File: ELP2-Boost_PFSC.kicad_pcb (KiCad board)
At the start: 2 copper layers, 130 x 150 mm, 44 parts, among them J1 Screw_Terminal_01x03, J2 Screw_Terminal_01x03, Q1 12n50C3, U1 UCC38050

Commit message: Placa refeita de acordo com pedidos do professor, sujeita a alteração
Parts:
- removed RV1: R_Potentiometer_Trim, ELP-Boost_PFC:Trimpot-10k
- added Rs1: 270m, Resistor_SMD:R_2512_6332Metric_Pad1.40x3.35mm_HandSolder, B.Cu at (144.2, 100.8)
- C1, C2, C3, C6: footprint Capacitor_THT:C_Disc_D5.0mm_W2.5mm_P2.50mm -> Capacitor_THT:C_Disc_D5.0mm_W2.5mm_P5.00mm
- C4: footprint Capacitor_THT:C_Rect_L9.0mm_W2.5mm_P7.50mm_MKT -> Capacitor_THT:C_Disc_D5.0mm_W2.5mm_P5.00mm
- C5: footprint Capacitor_THT:C_Rect_L13.5mm_W5.0mm_P10.00mm_FKS3_FKP3_MKS4 -> Capacitor_THT:C_Disc_D5.0mm_W2.5mm_P5.00mm
- C7: footprint Capacitor_THT:C_Rect_L7.2mm_W3.5mm_P5.00mm_FKS2_FKP2_MKS2_MKP2 -> Capacitor_THT:C_Rect_L31.5mm_W9.0mm_P27.50mm_MKS4
- R11, R12, R13: footprint Resistor_THT:R_Axial_DIN0207_L6.3mm_D2.5mm_P15.24mm_Horizontal -> Resistor_THT:R_Axial_DIN0207_L6.3mm_D2.5mm_P10.16mm_Horizontal
- TP1: value TestPoint -> Current_Sense
- moved TP1 86.7 mm to (137.0, 126.1), turned to 90 degrees
- moved C2 76.5 mm to (141.6, 122.1)
- moved R6 71.2 mm to (109.1, 106.4), turned to -90 degrees
- moved TP2 67.5 mm to (103.1, 107.1), turned to 0 degrees
- moved R5 64.3 mm to (138.8, 108.4), turned to 90 degrees
- moved C5 61.5 mm to (146.0, 117.4), turned to 0 degrees
- moved R7 61.1 mm to (109.0, 103.2), turned to 90 degrees
- moved J2 57.5 mm to (151.4, 66.1), turned to 90 degrees
- moved R3 55.4 mm to (148.0, 143.8), turned to -90 degrees
- moved R4 51.3 mm to (109.0, 89.5), turned to 90 degrees
- moved C4 51.1 mm to (145.9, 122.3)
- moved C1 45.8 mm to (142.7, 144.1), turned to -90 degrees
- moved R2 45.6 mm to (134.5, 154.6), turned to 180 degrees
- moved R9 40.3 mm to (151.0, 136.0), turned to 90 degrees
- moved R10 35.9 mm to (122.9, 121.8), turned to 90 degrees
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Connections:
- R6 pad 2: Net-(R6-Pad2) -> Earth
- TR1 pad 1: Net-(D6-A) -> /ZCD
- TR1 pad 5: Net-(D5-+) -> Earth
- TR1 pad 7: Earth -> Net-(D6-A)
- TR1 pad 9: /ZCD -> Net-(D5-+)
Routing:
- net /PFC/VO_SNS: track 168.8 -> 57.0 mm
- net /PFC/Current_Sense: track 119.5 -> 25.6 mm, vias 2 -> 0
- net Net-(D5-+): track 181.2 -> 90.3 mm
- net Earth: track 322.7 -> 253.1 mm, vias 2 -> 0
- net /PFC/Comp: track 76.2 -> 13.2 mm
- net /Vcc: track 49.0 -> 88.2 mm, vias 2 -> 0
- net Net-(D6-A): track 39.7 -> 67.2 mm
- net Net-(R1-Pad1): track 5.60 -> 32.7 mm
- net /ZCD: track 78.6 -> 53.2 mm
- net /PWM: track 26.6 -> 3.71 mm
- net /PFC/Zero_Cross: track 25.5 -> 9.57 mm
- net Net-(D7-K): track 13.7 -> 28.8 mm
- net /Out+: track 54.1 -> 68.0 mm
- net /CS: track 0.00 -> 10.0 mm
- net /PFC/Mult_In: track 61.7 -> 51.7 mm, vias 2 -> 0
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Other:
- board text removed: "Alimentação - Vcc"
- board text removed: "Compensador"
- board text removed: "Current Sense"
- board text removed: "Driver"
- board text removed: "Fechamento da Malha - 2,5V @ 400V Saída"
- board text removed: "Realimentação"
- board text removed: "Vo_SNS"
- board text removed: "Zero Cross"

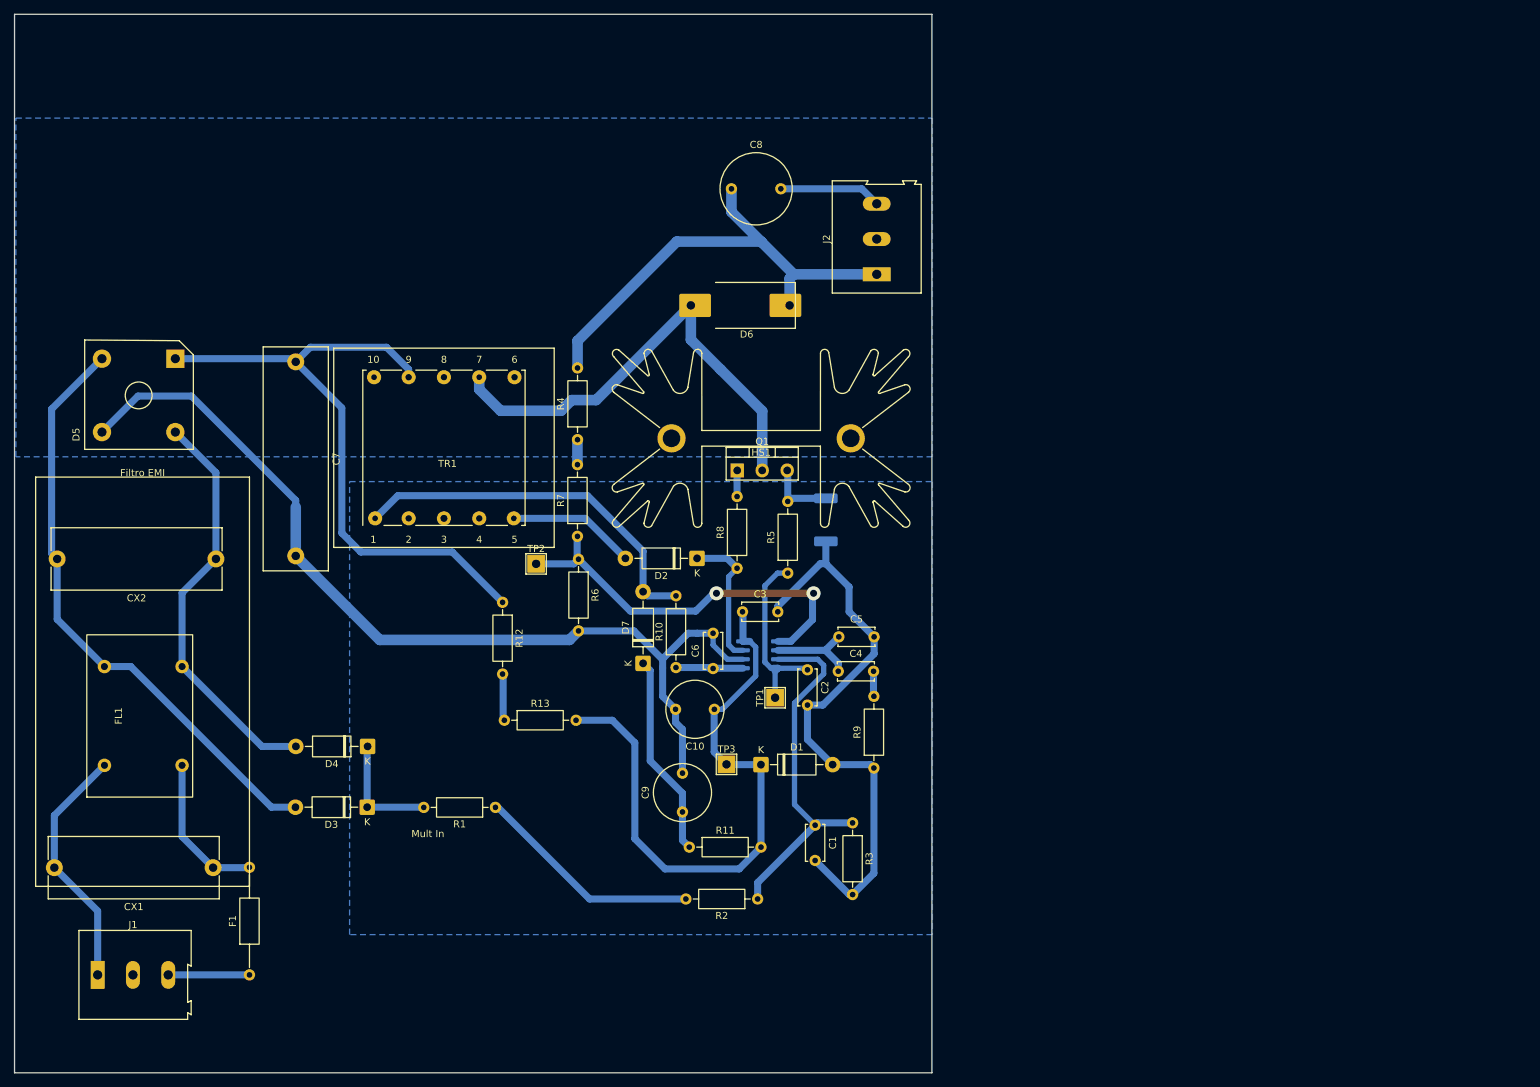
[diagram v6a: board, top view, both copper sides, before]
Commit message: Ajustes nos planos de referência e posição do shunt
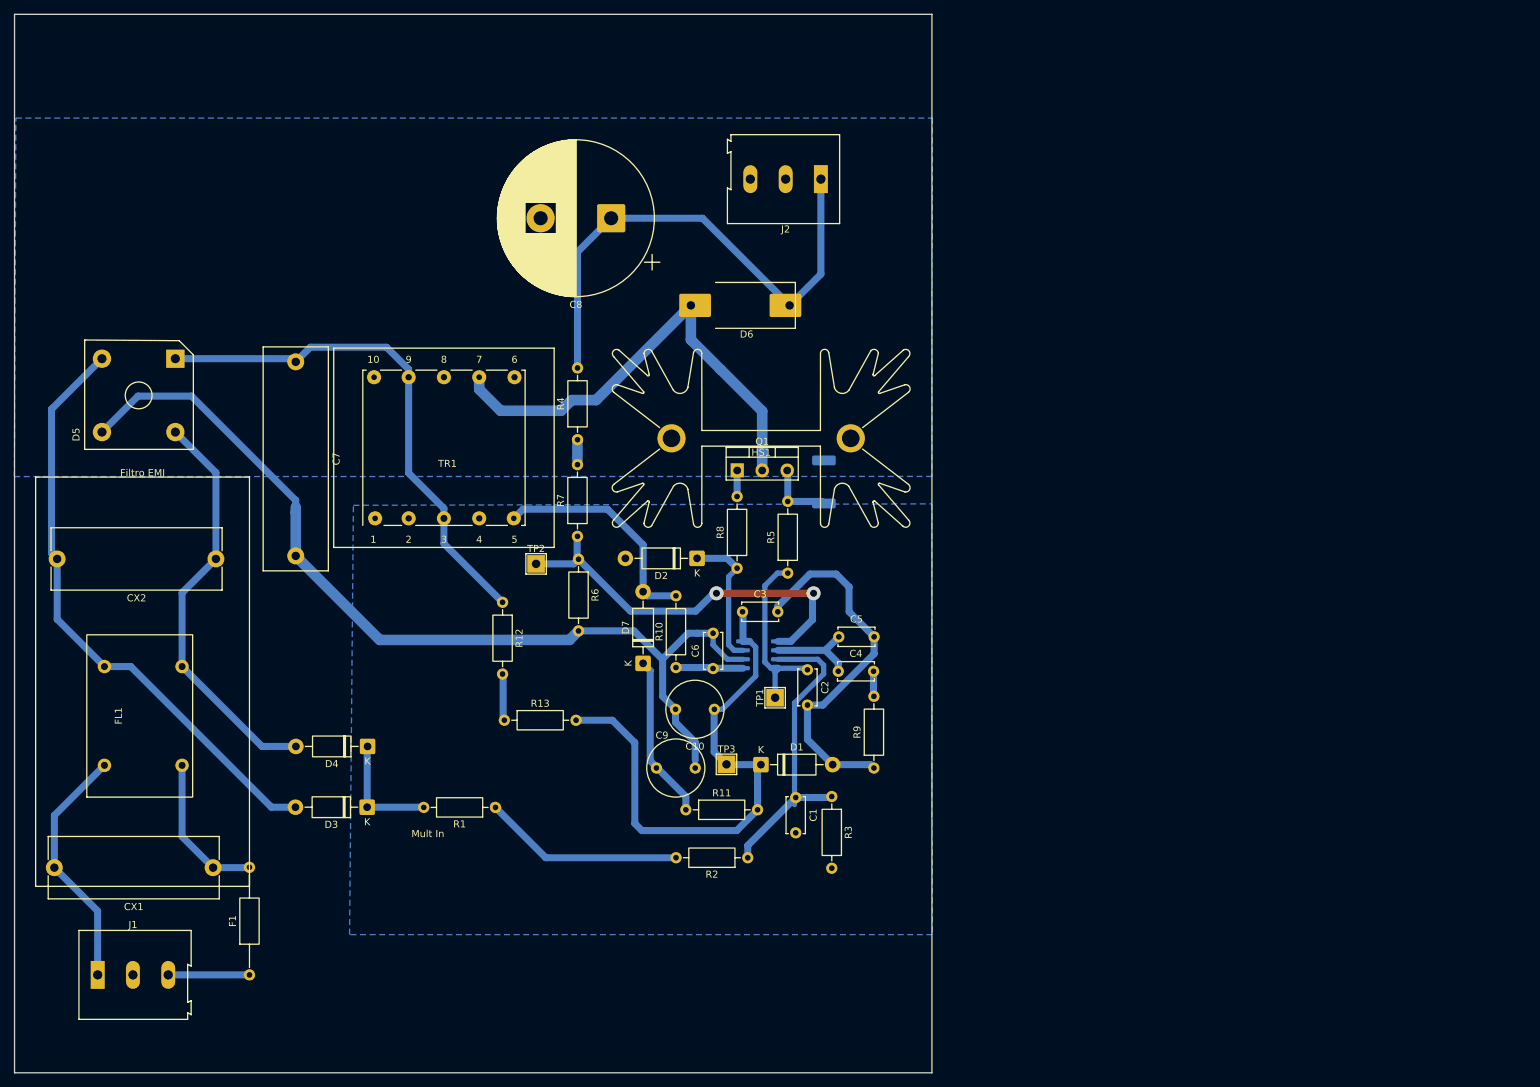
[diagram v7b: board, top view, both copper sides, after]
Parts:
- C8: footprint Capacitor_THT:C_Radial_D10.0mm_H20.0mm_P5.00mm -> Capacitor_THT:CP_Radial_D22.0mm_P10.00mm_SnapIn
- TP1: value Current_Sense -> TestPoint
- moved C8 18.5 mm to (113.8, 58.1), turned to 180 degrees
- moved J2 15.6 mm to (143.5, 52.6), turned to 180 degrees
- moved R2 6.02 mm to (133.1, 148.7)
- moved C9 5.88 mm to (121.2, 136.0), turned to 0 degrees
- moved Rs1 5.38 mm to (143.9, 95.5), turned to 90 degrees
- moved R11 5.31 mm to (124.3, 141.9)
- moved C1 4.79 mm to (139.9, 140.2)
- moved R3 4.76 mm to (145.0, 140.1)
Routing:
- net Earth: track 253.1 -> 188.5 mm
- net /ZCD: track 53.2 -> 32.5 mm
- net Net-(D5-+): track 90.3 -> 73.9 mm
- net /Vcc: track 88.2 -> 79.1 mm
- net /PFC/Mult_In: track 51.7 -> 44.8 mm
- net Net-(D7-K): track 28.8 -> 23.3 mm
- net /Out+: track 68.0 -> 73.3 mm
- net Net-(R1-Pad1): track 32.7 -> 29.2 mm

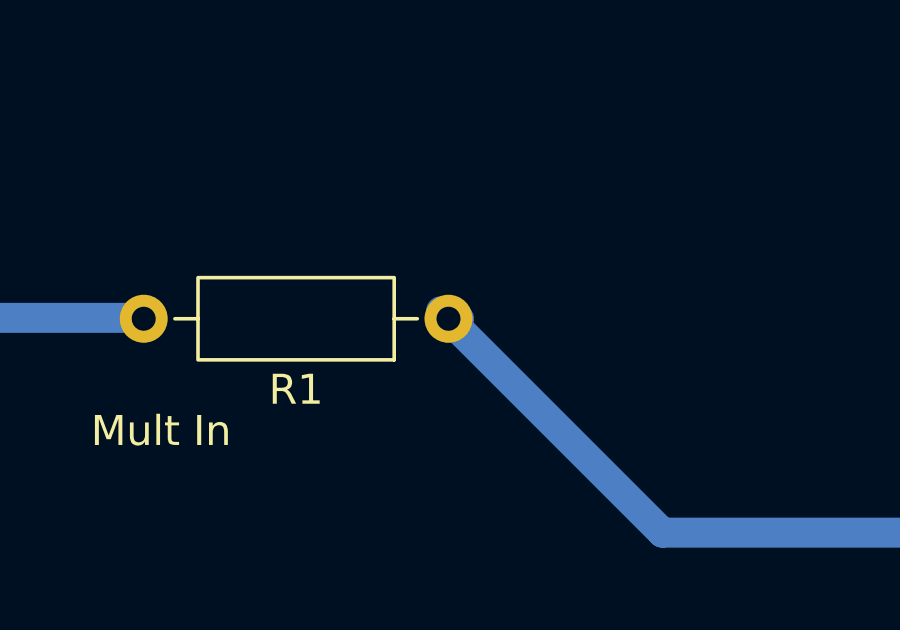
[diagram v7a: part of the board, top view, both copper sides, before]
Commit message: Small improvement to insulation
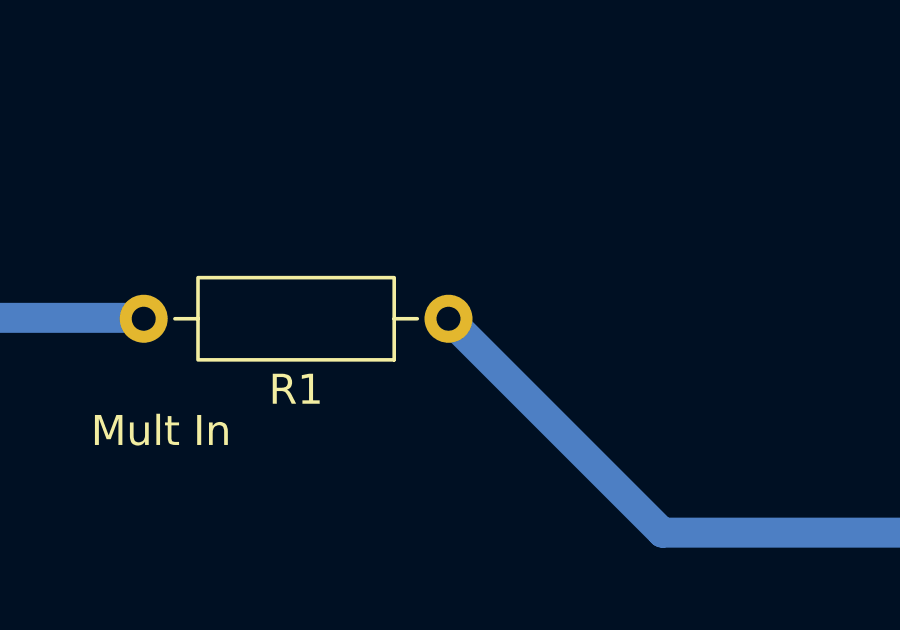
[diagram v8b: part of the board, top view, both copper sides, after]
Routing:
- net Net-(R1-Pad1): track 29.2 -> 28.5 mm
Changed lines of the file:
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@@
 			(net 21 "Net-(R1-Pad1)")
 			(pintype "passive")
+			(clearance 2)
 		)
 		(embedded_fonts no)
@@
 			(net 21 "Net-(R1-Pad1)")
 			(pintype "passive")
+			(clearance 2)
 		)
 		(pad "2" thru_hole circle
@@
 	)
 	(segment
-		(start 97.36 141.6)
-		(end 97.71 141.6)
-		(width 1)
-		(layer "B.Cu")
-		(net 21)
-	)
-	(segment
-		(start 97.11 141.35)
-		(end 97.36 141.6)
-		(width 1)
-		(layer "B.Cu")
-		(net 21)
-	)
-	(segment
 		(start 104.49 148.73)
 		(end 122.95 148.73)
@@
 	)
 	(zone
-		(net 17)
-		(net_name "Net-(D6-A)")
+		(net 8)
+		(net_name "Net-(D5-+)")
 		(layer "B.Cu")
 		(name "$teardrop_padvia$")
 		(hatch none 0.1)
-		(priority 30000)
+		(priority 30001)
 		(attr
 			(teardrop
@@
 		(polygon
 			(pts
-				(xy 135.91 91.915802) (xy 134.41 91.915802) (xy 134.225802 93.616676) (xy 135.16 93.851) (xy 136.094198 93.616676)
+				(xy 54.3 78.515) (xy 54.3 77.515) (xy 53.3 77.015) (xy 51.999 78.015) (xy 53.3 79.015)
 			)
 		)
 	)
 	(zone
-		(net 2)
-		(net_name "Earth")
+		(net 18)
+		(net_name "/Prot-EMI/P")
 		(layer "B.Cu")
-		(hatch edge 0.5)
-		(connect_pads
-			(clearance 0.75)
+		(name "$teardrop_padvia$")
+		(hatch none 0.1)
+		(priority 30002)
+		(attr
+			(teardrop
+				(type padvia)
+			)
 		)
-		(min_thickness 0.25)
+		(connect_pads yes
+			(clearance 0)
+		)
+		(min_thickness 0.0254)
 		(filled_areas_thickness no)
 		(fill yes
 			(thermal_gap 0.5)
 			(thermal_bridge_width 0.5)
+			(island_removal_mode 1)
+			(island_area_min 10)
 		)
 		(polygon
 			(pts
-				(xy 77.23 98.79) (xy 159.21 98.59) (xy 159.28 159.63) (xy 76.69 159.63)
+				(xy 52.97 165.835) (xy 52.97 164.835) (xy 51.98 164.345) (xy 50.989 165.335) (xy 51.98 166.325)
 			)
 		)
@@
 		(polygon
 			(pts
-				(xy 29.4 43.92) (xy 159.28 43.92) (xy 159.24 94.7) (xy 29.18 94.72)
+				(xy 77.23 98.79) (xy 159.21 98.59) (xy 159.28 159.63) (xy 76.69 159.63)
 			)
 		)
 	)
 	(zone
-		(net 8)
-		(net_name "Net-(D5-+)")
+		(net 2)
+		(net_name "Earth")
 		(layer "B.Cu")
-		(name "$teardrop_padvia$")
-		(hatch none 0.1)
-		(priority 30001)
-		(attr
-			(teardrop
-				(type padvia)
-			)
-		)
-		(connect_pads yes
-			(clearance 0)
+		(hatch edge 0.5)
+		(connect_pads
+			(clearance 0.75)
 		)
-		(min_thickness 0.0254)
+		(min_thickness 0.25)
 		(filled_areas_thickness no)
 		(fill yes
 			(thermal_gap 0.5)
 			(thermal_bridge_width 0.5)
-			(island_removal_mode 1)
-			(island_area_min 10)
 		)
 		(polygon
 			(pts
-				(xy 54.3 78.515) (xy 54.3 77.515) (xy 53.3 77.015) (xy 51.999 78.015) (xy 53.3 79.015)
+				(xy 29.4 43.92) (xy 159.28 43.92) (xy 159.24 94.7) (xy 29.18 94.72)
 			)
 		)
 	)
 	(zone
-		(net 18)
-		(net_name "/Prot-EMI/P")
+		(net 17)
+		(net_name "Net-(D6-A)")
 		(layer "B.Cu")
 		(name "$teardrop_padvia$")
 		(hatch none 0.1)
-		(priority 30002)
+		(priority 30000)
 		(attr
 			(teardrop
@@
 		(polygon
 			(pts
-				(xy 52.97 165.835) (xy 52.97 164.835) (xy 51.98 164.345) (xy 50.989 165.335) (xy 51.98 166.325)
+				(xy 135.91 91.915802) (xy 134.41 91.915802) (xy 134.225802 93.616676) (xy 135.16 93.851) (xy 136.094198 93.616676)
 			)
 		)
